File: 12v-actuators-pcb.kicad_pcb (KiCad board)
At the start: 2 copper layers, 109 x 60 mm, 105 parts, among them J1 12V_C_MOT, J10 ESC_35_2_P, J11 MOTOR_15_2, J12 ESC_35_2_S, J13 MOTOR_15_3, J14 690367280876, J2 3.5mm WR-TBL, J3 690367280676, J4 LCD_DEG, J5 CAN, J6 ESC_35_1_P, J7 LED_EN, J8 MOTOR_15_1, J9 ESC_35_1_S, Q1 G2302, Q2 G2302, Q3 G2302, Q4 G2302, Q5 G2302, Q6 SUM110P06-08L, Q7 2N7002, Q8 2N7002, U1 MCP2551-I-SN, U2 NUCLEO-F303K8, U3 WSEN-PDUS, U4 TCA9517DR, X1 ESC_Emax_Bullet_15A, X2 ESC_Emax_Bullet_15A, X3 ESC_Emax_Bullet_15A

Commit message: CDR 2025 version WIP
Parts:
- removed C15: 470pF, Capacitor_SMD:C_0603_1608Metric
- removed C3: 10uF, Capacitor_SMD:C_0805_2012Metric
- removed G*** (x5): LOGO, LOGO
- removed the J1 at (194.7, 106.4)
- removed the J4 at (154.1, 108.7)
- removed the J5 at (150.3, 103.7)
- removed REF** (x4): Mounting_Wuerth_WA-SMSI-M3_H1.5mm_9774015360, Mounting_Wuerth:Mounting_Wuerth_WA-SMSI-M3_H1.5mm_9774015360
- removed U2: NUCLEO-F303K8, ComponentsEvo:MODULE_NUCLEO-F303K8
- removed X1, X2, X3: ESC_Emax_Bullet_15A, ComponentsEvo:ESC_Emax_Bullet_15A
- added C27: 18pF, Capacitor_SMD:C_0603_1608Metric, F.Cu at (48.0, 43.6)
- added C28: 18pF, Capacitor_SMD:C_0603_1608Metric, F.Cu at (34.3, 49.6)
- added C29: 10nF, Capacitor_SMD:C_0603_1608Metric, F.Cu at (36.0, 52.9)
- added C30: 100nF, Capacitor_SMD:C_0603_1608Metric, F.Cu at (40.5, 43.6)
- added C31: 100nF, Capacitor_SMD:C_0603_1608Metric, F.Cu at (34.3, 52.9)
- added C32: 10nF, Capacitor_SMD:C_0603_1608Metric, F.Cu at (36.0, 49.6)
- added D10: ~, Diode_SMD:D_SOD-123F, F.Cu at (279.5, 126.1)
- added D11: ~, Diode_SMD:D_SOD-123F, F.Cu at (279.5, 132.9)
- added D12: ~, Diode_SMD:D_SOD-123F, F.Cu at (279.5, 96.1)
- added D13: ~, Diode_SMD:D_SOD-123F, F.Cu at (279.5, 88.4)
- added D14: ~, Diode_SMD:D_SOD-123F, F.Cu at (279.5, 80.6)
- added D15: ~, Diode_SMD:D_SOD-123F, F.Cu at (279.5, 155.9)
- added D16: ~, Diode_SMD:D_SOD-123F, F.Cu at (279.5, 148.1)
- added D17: ~, Diode_SMD:D_SOD-123F, F.Cu at (279.5, 140.1)
- added D18: ~, Diode_SMD:D_SOD-123F, F.Cu at (273.3, 50.1)
- added D9: D_Schottky, Diode_SMD:D_SOD-882, F.Cu at (214.0, 52.0)
- added J1: 690367280876, ConnectorsEvo:690367280876, F.Cu at (118.3, 68.4)
- added J1: 12V_C_MOT, ConnectorsEvo:691321100002, F.Cu at (137.0, 79.1)
- added J4: PROG, Connector_PinHeader_2.54mm:PinHeader_1x03_P2.54mm_Vertical, F.Cu at (66.8, 42.6)
- added J4: LCD_DEG, Connector_PinHeader_2.54mm:PinHeader_1x03_P2.54mm_Vertical, F.Cu at (142.0, 120.8)
- added J5: CAN, Connector_PinHeader_2.54mm:PinHeader_1x02_P2.54mm_Vertical, F.Cu at (205.0, 51.0)
- added J5: USB_B_Mini, ConnectorsEvo:USB_Mini-B_Wuerth_65100516121_Horizontal, F.Cu at (228.1, 50.5)
- added Q10: G2302, Package_TO_SOT_SMD:SOT-23, F.Cu at (276.4, 88.4)
- added Q11: G2302, Package_TO_SOT_SMD:SOT-23, F.Cu at (276.2, 80.6)
- added Q12: G2302, Package_TO_SOT_SMD:SOT-23, F.Cu at (276.3, 155.9)
- added Q13: G2302, Package_TO_SOT_SMD:SOT-23, F.Cu at (276.3, 148.1)
- added Q14: G2302, Package_TO_SOT_SMD:SOT-23, F.Cu at (276.0, 140.1)
- added Q15: G2302, Package_TO_SOT_SMD:SOT-23, F.Cu at (276.3, 96.1)
- added Q16: G2302, Package_TO_SOT_SMD:SOT-23, F.Cu at (149.0, 52.0)
- added Q17: G2302, Package_TO_SOT_SMD:SOT-23, F.Cu at (270.0, 50.1)
- added Q9: G2302, Package_TO_SOT_SMD:SOT-23, F.Cu at (276.3, 132.9)
- added R33: 10k, Resistor_SMD:R_0603_1608Metric, F.Cu at (273.5, 126.1)
- added R34: 1k, Resistor_SMD:R_0603_1608Metric, F.Cu at (271.5, 132.9)
- added R35: 10k, Resistor_SMD:R_0603_1608Metric, F.Cu at (273.3, 132.9)
- added R36: 1k, Resistor_SMD:R_0603_1608Metric, F.Cu at (271.8, 96.1)
- added R37: 1k, Resistor_SMD:R_0603_1608Metric, F.Cu at (271.8, 88.4)
- added R38: 1k, Resistor_SMD:R_0603_1608Metric, F.Cu at (271.5, 80.6)
- added R39: 1k, Resistor_SMD:R_0603_1608Metric, F.Cu at (271.8, 155.9)
- added R40: 1k, Resistor_SMD:R_0603_1608Metric, F.Cu at (271.8, 148.1)
- added R41: 1k, Resistor_SMD:R_0603_1608Metric, F.Cu at (271.3, 140.1)
- added R42: 10k, Resistor_SMD:R_0603_1608Metric, F.Cu at (273.3, 80.6)
- added R43: 10k, Resistor_SMD:R_0603_1608Metric, F.Cu at (273.5, 155.9)
- added R44: 10k, Resistor_SMD:R_0603_1608Metric, F.Cu at (273.5, 148.1)
- added R45: 10k, Resistor_SMD:R_0603_1608Metric, F.Cu at (273.0, 140.1)
- added R46: 10k, Resistor_SMD:R_0603_1608Metric, F.Cu at (273.5, 88.4)
- added R47: 10k, Resistor_SMD:R_0603_1608Metric, F.Cu at (273.5, 96.1)
- added R48: 10k, Resistor_SMD:R_0603_1608Metric, F.Cu at (152.0, 45.0)
- added R49: 0, Resistor_SMD:R_0603_1608Metric, F.Cu at (152.0, 48.0)
- added R50: 22, Resistor_SMD:R_0603_1608Metric, F.Cu at (198.0, 58.0)
- added R51: 1k, Resistor_SMD:R_0603_1608Metric, F.Cu at (265.5, 50.1)
- added R52: 10k, Resistor_SMD:R_0603_1608Metric, F.Cu at (267.3, 50.1)
- added R53: 0, Resistor_SMD:R_0402_1005Metric, F.Cu at (55.0, 50.6)
- added R54: 0, Resistor_SMD:R_0402_1005Metric, F.Cu at (41.0, 61.6)
- added R55: 0, Resistor_SMD:R_0402_1005Metric, F.Cu at (42.3, 61.6)
- added R56: 0, Resistor_SMD:R_0402_1005Metric, F.Cu at (55.0, 56.9)
- added R57: 0, Resistor_SMD:R_0402_1005Metric, F.Cu at (55.0, 58.1)
- added R58: 0, Resistor_SMD:R_0402_1005Metric, F.Cu at (48.5, 61.6)
- added R59: 0, Resistor_SMD:R_0402_1005Metric, F.Cu at (47.3, 61.6)
- added R60: 0, Resistor_SMD:R_0402_1005Metric, F.Cu at (46.0, 61.6)
- added R61: 0, Resistor_SMD:R_0402_1005Metric, F.Cu at (27.5, 49.1)
- added R62: 0, Resistor_SMD:R_0402_1005Metric, F.Cu at (43.5, 61.6)
- added R63: 0, Resistor_SMD:R_0402_1005Metric, F.Cu at (44.8, 61.6)
- added R64: 0, Resistor_SMD:R_0402_1005Metric, F.Cu at (27.5, 50.4)
- added R65: 0, Resistor_SMD:R_0402_1005Metric, F.Cu at (27.5, 51.6)
- added R66: 0, Resistor_SMD:R_0402_1005Metric, F.Cu at (27.5, 52.9)
- added R67: 0, Resistor_SMD:R_0402_1005Metric, F.Cu at (55.0, 55.6)
- added R68: 0, Resistor_SMD:R_0402_1005Metric, F.Cu at (55.0, 54.4)
- added R69: 0, Resistor_SMD:R_0402_1005Metric, F.Cu at (55.0, 53.1)
- added R70: 0, Resistor_SMD:R_0402_1005Metric, F.Cu at (55.0, 49.4)
- added R71: 0, Resistor_SMD:R_0402_1005Metric, F.Cu at (43.0, 37.1)
- added R72: 0, Resistor_SMD:R_0402_1005Metric, F.Cu at (41.8, 37.1)
- added R73: 0, Resistor_SMD:R_0402_1005Metric, F.Cu at (55.0, 51.9)
- added R74: 0, Resistor_SMD:R_0402_1005Metric, F.Cu at (27.5, 55.4)
- added R75: 0, Resistor_SMD:R_0402_1005Metric, F.Cu at (27.5, 54.1)
- added R76: 0, Resistor_SMD:R_0402_1005Metric, F.Cu at (55.0, 48.1)
- added R77: 10k, Resistor_SMD:R_0402_1005Metric, F.Cu at (233.0, 59.0)
- added R78: 0, Resistor_SMD:R_0402_1005Metric, F.Cu at (40.5, 37.1)
- added R79: 0, Resistor_SMD:R_0402_1005Metric, F.Cu at (76.4, 45.8)
- added R80: 0, Resistor_SMD:R_0402_1005Metric, F.Cu at (76.4, 47.8)
- added R81: 0, Resistor_SMD:R_0402_1005Metric, F.Cu at (76.4, 49.8)
- added SW1: 435431019840, ComponentsEvo:435431019840, F.Cu at (220.0, 46.0)
- added TP1: TestPoint_Small, TestPoint:TestPoint_Pad_D1.0mm, F.Cu at (39.5, 32.4)
- added TP10: TestPoint_Small, TestPoint:TestPoint_Pad_D1.0mm, F.Cu at (64.3, 51.6)
- added TP11: TestPoint_Small, TestPoint:TestPoint_Pad_D1.0mm, F.Cu at (48.3, 32.4)
- added TP12: TestPoint_Small, TestPoint:TestPoint_Pad_D1.0mm, F.Cu at (41.8, 68.6)
- added TP13: TestPoint_Small, TestPoint:TestPoint_Pad_D1.0mm, F.Cu at (64.3, 54.1)
- added TP14: TestPoint_Small, TestPoint:TestPoint_Pad_D1.0mm, F.Cu at (22.0, 50.6)
- added TP2: TestPoint_Small, TestPoint:TestPoint_Pad_D1.0mm, F.Cu at (41.0, 29.9)
- added TP3: TestPoint_Small, TestPoint:TestPoint_Pad_D1.0mm, F.Cu at (22.0, 47.9)
- added TP4: TestPoint_Small, TestPoint:TestPoint_Pad_D1.0mm, F.Cu at (22.0, 53.4)
- added TP5: TestPoint_Small, TestPoint:TestPoint_Pad_D1.0mm, F.Cu at (41.8, 66.4)
- added TP6: TestPoint_Small, TestPoint:TestPoint_Pad_D1.0mm, F.Cu at (38.8, 68.6)
- added TP7: TestPoint_Small, TestPoint:TestPoint_Pad_D1.0mm, F.Cu at (44.8, 68.6)
- added TP8: TestPoint_Small, TestPoint:TestPoint_Pad_D1.0mm, F.Cu at (45.3, 32.4)
- added TP9: TestPoint_Small, TestPoint:TestPoint_Pad_D1.0mm, F.Cu at (42.5, 32.4)
- added U5: STM32G474CEUx, Package_DFN_QFN:QFN-48-1EP_7x7mm_P0.5mm_EP5.6x5.6mm, F.Cu at (43.8, 52.4)
- added U6: TPS82130, Goldorak:MicroSiP, F.Cu at (56.8, 119.9)
- added U7: AMS1117-3.3, Package_TO_SOT_SMD:SOT-89-3, F.Cu at (209.0, 62.0)
- added Y1: 16 MHz, Crystal:Crystal_SMD_5032-4Pin_5.0x3.2mm, F.Cu at (44.3, 43.6)
- C12: value 470pF -> 10uF
- C14, C4: value 100nF -> 10uF
- C7: value 470pF -> 430pF
- C9: value 100nF -> 22uF
- D1: value ~ -> D_Schottky; footprint Diode_SMD:D_SOD-123F -> Diode_SMD:D_SOD-882
- J10: value ESC_35_2_P -> ESC_35_1_P
- J11: value MOTOR_15_2 -> 690367280876; footprint Connector_PinHeader_2.54mm:PinHeader_1x03_P2.54mm_Vertical -> ConnectorsEvo:690367280876
- J13: value MOTOR_15_3 -> STLINK; footprint Connector_PinHeader_2.54mm:PinHeader_1x03_P2.54mm_Vertical -> ConnectorsEvo:SAMTEC_FTSH-107-01-L-DV-K
- J7: value LED_EN -> RGBA_LEDs; footprint Connector_PinHeader_2.54mm:PinHeader_1x02_P2.54mm_Vertical -> Connector_PinHeader_2.54mm:PinHeader_1x03_P2.54mm_Vertical
- J8: value MOTOR_15_1 -> CAN
- R12: value 22 -> 1k
- R3: value 22 -> 100k
- R4: value 1k -> 523k
- R5: value 10k -> 100k
- R7: value 22 -> 10k
- moved D2 147.8 mm to (279.5, 111.6), turned to 90 degrees
- moved D3 147.2 mm to (279.5, 119.1), turned to -90 degrees
- moved Q2 145.9 mm to (276.3, 111.6), turned to 0 degrees
- moved Q3 143.9 mm to (276.3, 119.1), turned to 0 degrees
- moved R9 142.0 mm to (273.5, 111.6)
- moved R8 141.7 mm to (271.8, 111.6)
- moved R13 139.8 mm to (273.5, 119.1)
- moved R11 139.6 mm to (271.8, 119.1), turned to 90 degrees
- moved D4 137.0 mm to (278.8, 70.6), turned to 90 degrees
- moved C23 136.0 mm to (231.0, 40.0), turned to 0 degrees
- moved D5 135.8 mm to (279.5, 104.1), turned to 90 degrees
- moved Q4 134.6 mm to (275.5, 70.6), turned to 0 degrees
- moved Q5 132.0 mm to (276.3, 104.1), turned to 0 degrees
- moved R15 131.7 mm to (272.8, 70.6)
- moved R14 131.4 mm to (271.0, 70.6)
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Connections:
- net /A_PRES renamed /Capteurs/A_PRES
- C1 pad 2: +5V -> +5VL
- C12 pad 1: Net-(X2-S) -> +5VL
- C14 pad 1: GNDPWR -> +3.3V
- C14 pad 2: /PWR_12V -> GND
- C20 pad 1: +5V -> +5VL
- C24 pad 1: +5V -> +5VL
- C4 pad 1: GNDPWR -> /VBATT_12V
- C4 pad 2: /PWR_12V -> GND
- C7 pad 1: Net-(X1-S) -> Net-(U6-SS/TR)
- C7 pad 2: GND -> GNDPWR
- C9 pad 1: GNDPWR -> +5VP
- C9 pad 2: /PWR_12V -> GNDPWR
- D1 pad 1: /PWR_12V -> +5VL
- D1 pad 2: Net-(D1-A) -> /5V_CAN
- J11 pad 1: Net-(J11-Pin_1) -> /PWR_12V
- J11 pad 2: Net-(J11-Pin_2) -> /Actionneurs/12V_EV8
- J11 pad 3: Net-(J11-Pin_3) -> /PWR_12V
- J13 pad 1: Net-(J13-Pin_1) -> unconnected-(J13-Pin_1-Pad1)
- J13 pad 2: Net-(J13-Pin_2) -> unconnected-(J13-Pin_2-Pad2)
- J13 pad 3: Net-(J13-Pin_3) -> +3.3V
- J14 pad 7: /PWR_12V -> /VBATT_12V
- J6 pad 2: GNDPWR -> Net-(J6-Pin_2)
- J7 pad 1: Net-(D1-A) -> +5VP
- J7 pad 2: /PWR_12V -> /DATA_LED
- J8 pad 1: Net-(J8-Pin_1) -> /CAN+
- J8 pad 2: Net-(J8-Pin_2) -> /CAN-
- J8 pad 3: Net-(J8-Pin_3) -> /5V_CAN
- Q1 pad 3: Net-(D1-A) -> /Actionneurs/12V_EV4
- R12 pad 1: /DS_M3 -> Net-(Q1-G)
- R12 pad 2: Net-(X3-S) -> /EV_4
- R25 pad 1: +5V -> +5VL
- R26 pad 1: +5V -> +5VL
- R3 pad 1: /DS_M1 -> +5VP
- R3 pad 2: Net-(X1-S) -> Net-(U6-PG)
- R4 pad 1: Net-(Q1-G) -> Net-(U6-FB)
- R4 pad 2: /LED_EN -> +5VP
- R5 pad 1: Net-(Q1-G) -> GNDPWR
- R5 pad 2: GNDPWR -> Net-(U6-FB)
- R7 pad 1: /DS_M2 -> GNDPWR
- R7 pad 2: Net-(X2-S) -> +5VL
- U1 pad 1: /CAN_TD -> /CAN_TX
- U1 pad 3: +5V -> +5VL
- U1 pad 4: /CAN_RD -> /CAN_RX
- U3 pad 5: +5V -> +5VL
- U4 pad 8: +5V -> +5VL
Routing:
- net GND: track 334.5 -> 0.00 mm, vias 69 -> 0
- net +5V: track 149.1 -> 0.00 mm, vias 6 -> 0
- net /PWR_12V: track 121.8 -> 0.00 mm, vias 7 -> 0
- net /VBATT_12V: track 116.2 -> 0.00 mm, vias 3 -> 0
- net +3.3V: track 111.6 -> 0.00 mm, vias 3 -> 0
- net /EV_P: track 87.7 -> 0.00 mm
- net /DS_COMP: track 77.7 -> 0.00 mm, vias 3 -> 0
- net GNDPWR: track 72.0 -> 0.00 mm, vias 13 -> 0
- net /DS_M1: track 64.2 -> 0.00 mm, vias 2 -> 0
- net /EV_3: track 62.1 -> 0.00 mm
- net /CAN_TD: track 57.1 -> 0.00 mm, vias 1 -> 0
- net /SDA: track 57.0 -> 0.00 mm
- net /EV_2: track 56.6 -> 0.00 mm
- net Net-(X1-S): track 55.3 -> 0.00 mm, vias 1 -> 0
- net /EV_1: track 49.9 -> 0.00 mm
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- removed copper zone on F.Cu, net /PWR_12V
- removed copper zone on F.Cu, net /VBATT_12V
- removed copper zone on B.Cu, net GND
- removed copper zone on F.Cu, net GND
- removed copper zone on B.Cu, net GNDPWR
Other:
- board size 109 x 60 mm -> 100 x 60 mm
- board text removed: "+"
- board text removed: "-"
- board text removed: "12V BATT"
- board text removed: "24V"
- board text removed: "5V"
- board text removed: "AU Switched 12V"
- board text removed: "BATT"
- board text removed: "BRUSHLESS MOTOR OUTPUT"
- board text removed: "CANH"
- board text removed: "CANL"
- board text removed: "COMP"
- board text removed: "Carte pneumatique / Actionneurs 12V"
- board text removed: "Carte pneumatique Actionneurs 12V"
- board text removed: "DROITE"
- board text removed: "Design: Raphaël Casimir Review: Audran Caron Thanks: kmikaz"
- board text removed: "EN"
- board text removed: "ESC"
- board text removed: "EV1"
- board text removed: "EV2"
- board text removed: "EV3"
- board text removed: "G"
- board text removed: "GAUCHE"
- board text removed: "GND"
- board text removed: "G_L"
- board text removed: "G_P"
- board text removed: "H-BRG"
- board text removed: "IN"
- board text removed: "LED"
- board text removed: "MILIEU"
- board text removed: "OUT"
- board text removed: "PRG"
- board text removed: "S"
- board text removed: "TURB"
- board text removed: "VCC"
- board text removed: "X 5 AU G X X"
- board text removed: "clavier"

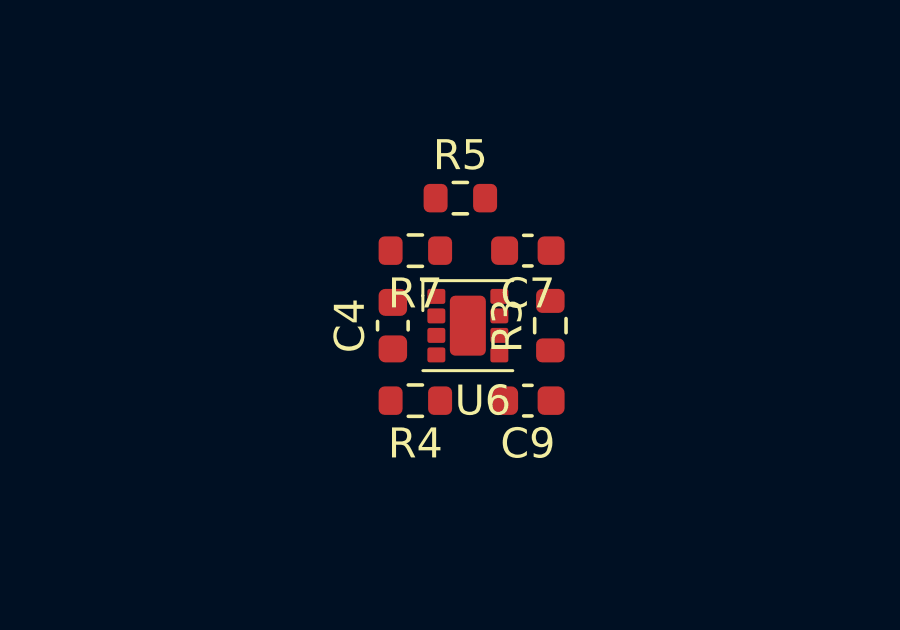
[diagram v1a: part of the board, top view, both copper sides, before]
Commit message: split des cartes
Todo: sync routage et ajout trou de fixation
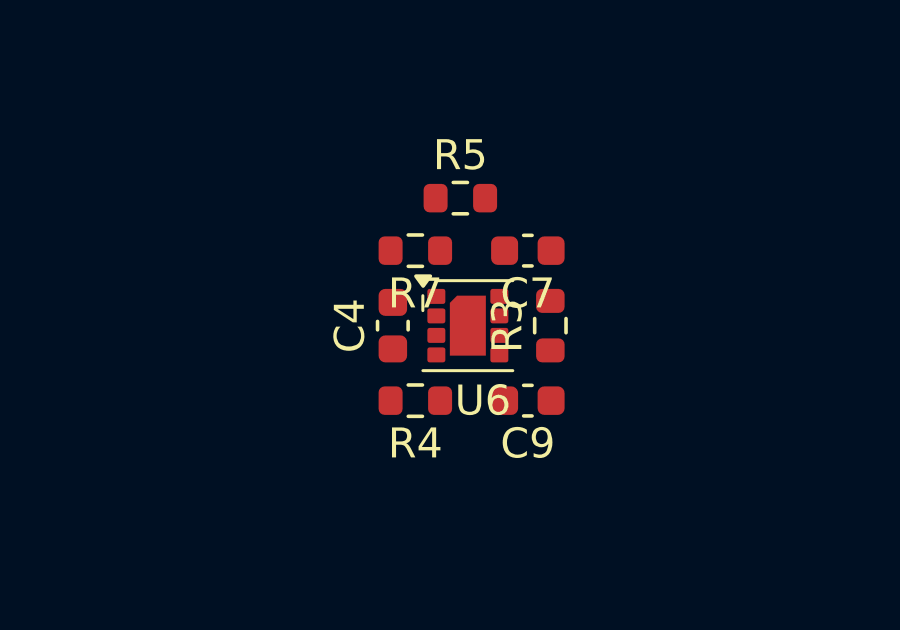
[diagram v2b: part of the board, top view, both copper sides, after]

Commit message: ajout d'une lib projet et synchro PCB
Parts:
- removed C31: 100nF, Capacitor_SMD:C_0603_1608Metric
- removed C32: 10nF, Capacitor_SMD:C_0603_1608Metric
- removed D11: ~, Diode_SMD:D_SOD-123F
- removed the J1 at (118.3, 68.4)
- removed the J4 at (66.8, 42.6)
- removed the J5 at (205.0, 51.0)
- removed Q9: G2302, Package_TO_SOT_SMD:SOT-23
- removed R34: 1k, Resistor_SMD:R_0603_1608Metric
- removed R35: 10k, Resistor_SMD:R_0603_1608Metric
- removed TP10, TP11, TP12, TP13, TP14, TP9: TestPoint_Small, TestPoint:TestPoint_Pad_D1.0mm
- removed U7: AMS1117-3.3, Package_TO_SOT_SMD:SOT-89-3
- added C15: 18pF, Capacitor_SMD:C_0603_1608Metric, F.Cu at (69.1, 157.0)
- added C3: 100nF, Capacitor_SMD:C_0603_1608Metric, F.Cu at (69.1, 154.5)
- added D19: ~, Diode_SMD:D_SOD-123F, F.Cu at (53.6, 172.9)
- added J15: BOOT0, Connector_PinHeader_2.54mm:PinHeader_1x02_P2.54mm_Vertical, F.Cu at (73.4, 155.6)
- added J16: 690367280876, ConnectorsEvo:690367280876, F.Cu at (39.4, 179.2)
- added J17: 690367280876, ConnectorsEvo:690367280676, F.Cu at (56.5, 157.7)
- added J18: 690367280876, ConnectorsEvo:690367280676, F.Cu at (56.5, 166.7)
- added J19: Alim EV, Connector_PinSocket_2.54mm:PinSocket_1x02_P2.54mm_Vertical, F.Cu at (34.8, 155.6)
- added J20: Alim EV, Connector_PinSocket_2.54mm:PinSocket_1x02_P2.54mm_Vertical, F.Cu at (39.4, 155.6)
- added J21: Alim EV, Connector_PinSocket_2.54mm:PinSocket_1x02_P2.54mm_Vertical, F.Cu at (44.0, 155.6)
- added J22: Alim EV, Connector_PinSocket_2.54mm:PinSocket_1x02_P2.54mm_Vertical, F.Cu at (48.5, 155.6)
- added J23: Alim EV, Connector_PinSocket_2.54mm:PinSocket_1x02_P2.54mm_Vertical, F.Cu at (34.8, 162.7)
- added J24: Alim EV, Connector_PinSocket_2.54mm:PinSocket_1x02_P2.54mm_Vertical, F.Cu at (39.4, 162.7)
- added J25: Alim EV, Connector_PinSocket_2.54mm:PinSocket_1x02_P2.54mm_Vertical, F.Cu at (44.0, 162.7)
- added J26: Alim EV, Connector_PinSocket_2.54mm:PinSocket_1x02_P2.54mm_Vertical, F.Cu at (48.5, 162.7)
- added J27: Alim EV, Connector_PinSocket_2.54mm:PinSocket_1x02_P2.54mm_Vertical, F.Cu at (34.8, 169.8)
- added J28: Alim EV, Connector_PinSocket_2.54mm:PinSocket_1x02_P2.54mm_Vertical, F.Cu at (39.4, 169.8)
- added J29: Alim EV, Connector_PinSocket_2.54mm:PinSocket_1x02_P2.54mm_Vertical, F.Cu at (44.0, 169.8)
- added J30: Alim EV, Connector_PinSocket_2.54mm:PinSocket_1x02_P2.54mm_Vertical, F.Cu at (48.5, 169.8)
- added Q18: G2302, Package_TO_SOT_SMD:SOT-23, F.Cu at (57.3, 177.0)
- added R82: 10k, Resistor_SMD:R_0603_1608Metric, F.Cu at (69.1, 159.5)
- added R83: 0, Resistor_SMD:R_0402_1005Metric, F.Cu at (65.6, 154.2)
- added R84: 0, Resistor_SMD:R_0402_1005Metric, F.Cu at (65.6, 156.2)
- added R85: 0, Resistor_SMD:R_0402_1005Metric, F.Cu at (65.6, 158.2)
- added R86: 0, Resistor_SMD:R_0402_1005Metric, F.Cu at (65.6, 160.2)
- added R87: 1k, Resistor_SMD:R_0603_1608Metric, F.Cu at (52.8, 175.8)
- added R88: 10k, Resistor_SMD:R_0603_1608Metric, F.Cu at (52.8, 178.3)
- added U2: TCA9517DR, Package_SO:SOIC-8_3.9x4.9mm_P1.27mm, F.Cu at (71.3, 164.1)
- C12: value 10uF -> 100nF
- C14: value 10uF -> 18pF
- C20: value 220nF -> 10nF
- C21: value 15nF -> 100nF
- C24: value 100nF -> 220nF
- C25: value 100nF -> 10nF
- C26: value 1uF -> 15nF; footprint Capacitor_SMD:C_0805_2012Metric -> Capacitor_SMD:C_0603_1608Metric
- C27: value 18pF -> 100nF
- C28: value 18pF -> 1uF; footprint Capacitor_SMD:C_0603_1608Metric -> Capacitor_SMD:C_0805_2012Metric
- C29: value 10nF -> 10uF
- C30: value 100nF -> 10uF
- J1: value 12V_C_MOT -> 690367280876; footprint ConnectorsEvo:691321100002 -> ConnectorsEvo:690367280676
- J11: footprint ConnectorsEvo:690367280876 -> ConnectorsEvo:690367280676
- J13: value STLINK -> Alim Pompe; footprint ConnectorsEvo:SAMTEC_FTSH-107-01-L-DV-K -> Connector_PinHeader_2.54mm:PinHeader_1x02_P2.54mm_Vertical
- J4: value LCD_DEG -> STLINK; footprint Connector_PinHeader_2.54mm:PinHeader_1x03_P2.54mm_Vertical -> ConnectorsEvo:SAMTEC_FTSH-107-01-L-DV-K
- J8: footprint Connector_PinHeader_2.54mm:PinHeader_1x03_P2.54mm_Vertical -> Connector_PinHeader_2.54mm:PinHeader_1x04_P2.54mm_Vertical
- R27: value 22 -> 10k
- R29: value 10k -> 0; footprint Resistor_SMD:R_0603_1608Metric -> Resistor_SMD:R_0402_1005Metric
- R3: value 100k -> 10k
- R30, R31: value 100k -> 0; footprint Resistor_SMD:R_0603_1608Metric -> Resistor_SMD:R_0402_1005Metric
- R32: value 22 -> 0; footprint Resistor_SMD:R_0603_1608Metric -> Resistor_SMD:R_0402_1005Metric
- R4: value 523k -> 100k
- R5: value 100k -> 523k
- R64, R80: value 0 -> 22; footprint Resistor_SMD:R_0402_1005Metric -> Resistor_SMD:R_0603_1608Metric
- R7: value 10k -> 100k
- R77: value 10k -> 0
- R78, R79: value 0 -> 100k; footprint Resistor_SMD:R_0402_1005Metric -> Resistor_SMD:R_0603_1608Metric
- R81: value 0 -> 10k
- U4: value TCA9517DR -> STM32G474CEUx; footprint Package_SO:SOIC-8_3.9x4.9mm_P1.27mm -> Package_DFN_QFN:QFN-48-1EP_7x7mm_P0.5mm_EP5.6x5.6mm
- U5: value STM32G474CEUx -> AMS1117-3.3; footprint Package_DFN_QFN:QFN-48-1EP_7x7mm_P0.5mm_EP5.6x5.6mm -> Package_TO_SOT_SMD:SOT-89-3
- U6: footprint Goldorak:MicroSiP -> 12V-actuators_pcb:MicroSiP
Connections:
- net /Arrêt d'urgence/SW_AU/2 renamed /Alim et Arrêt d'urgence/SW_AU/2
- C14 pad 1: +3.3V -> GND
- C14 pad 2: GND -> Net-(U4-PF0)
- C20 pad 1: +5VL -> +3.3V
- C21 pad 1: Net-(U3-VOUT) -> +3.3V
- C22 pad 1: /Capteurs/A_PRES -> Net-(U3-VOUT)
- C25 pad 1: GND -> +3.3V
- C25 pad 2: Net-(C25-Pad2) -> GND
- C26 pad 1: GND -> /MCU et capteurs/A_PRES
- C26 pad 2: /A_TEMP -> GND
- C27 pad 2: Net-(U5-PF0) -> Net-(C27-Pad2)
- C28 pad 2: Net-(U5-PF1) -> /MCU et capteurs/A_TEMP
- C29 pad 1: +3.3V -> +5VL
- C4 pad 2: GND -> GNDPWR
- D1 pad 2: /5V_CAN -> /5L
- J11 pad 2: /Actionneurs/12V_EV8 -> GNDPWR
- J11 pad 3: /PWR_12V -> /EV_9
- J11 pad 4: /Actionneurs/12V_EV9 -> /EV_10
- J11 pad 5: /PWR_12V -> /EV_11
- J11 pad 6: /Actionneurs/12V_EV10 -> unconnected-(J11-Pad6)
- J13 pad 1: unconnected-(J13-Pin_1-Pad1) -> /PWR_12V
- J13 pad 2: unconnected-(J13-Pin_2-Pad2) -> /Actionneurs/12V_VAC
- J14 pad 2: /Actionneurs/12V_EV1 -> GNDPWR
- J14 pad 3: /PWR_12V -> /VBATT_12V
- J14 pad 4: /Actionneurs/12V_EV2 -> /EV_P
- J14 pad 5: /PWR_12V -> /EV_1
- J14 pad 6: /Actionneurs/12V_EV3 -> /EV_2
- J14 pad 7: /VBATT_12V -> /EV_3
- J14 pad 8: /Actionneurs/12V_EVP -> /EV_4
- J3 pad 3: +5V -> /5L
- J4 pad 1: /SW_AU -> unconnected-(J4-Pin_1-Pad1)
- J4 pad 2: GNDPWR -> unconnected-(J4-Pin_2-Pad2)
- J4 pad 3: /LCD_EN -> +3.3V
- J8 pad 1: /CAN+ -> /5L
- J8 pad 2: /CAN- -> GND
- J8 pad 3: /5V_CAN -> /CANH
- R1 pad 1: /CAN+ -> /CANH
- R2 pad 2: /CAN- -> /CANL
- R25 pad 1: +5VL -> +3.3V
- R25 pad 2: /Capteurs/SDA_5 -> /MCU et capteurs/SCL
- R26 pad 1: +5VL -> +3.3V
- R26 pad 2: /Capteurs/SCL_5 -> /MCU et capteurs/SDA
- R27 pad 1: Net-(U3-VOUT) -> +5VL
- R27 pad 2: /Capteurs/A_PRES -> /MCU et capteurs/SDA_5
- R28 pad 1: +3.3V -> +5VL
- R28 pad 2: /SCL -> /MCU et capteurs/SCL_5
- R29 pad 1: +3.3V -> /EV_4
- R29 pad 2: /SDA -> Net-(U4-PC15)
- R3 pad 1: +5VP -> GNDPWR
- R3 pad 2: Net-(U6-PG) -> +5VL
- R30 pad 1: +3.3V -> /EV_1
- R30 pad 2: Net-(C25-Pad2) -> Net-(U4-PB0)
- R31 pad 1: +3.3V -> /EV_2
- R31 pad 2: Net-(C25-Pad2) -> Net-(U4-PB1)
- R32 pad 1: Net-(C25-Pad2) -> /EV_3
- R32 pad 2: /A_TEMP -> Net-(U4-PB2)
- R4 pad 1: Net-(U6-FB) -> +5VP
- R4 pad 2: +5VP -> Net-(U6-PG)
- R5 pad 1: GNDPWR -> Net-(U6-FB)
- R5 pad 2: Net-(U6-FB) -> +5VP
- R53 pad 1: /SDA -> /MCU et capteurs/SWO
- R53 pad 2: Net-(U5-PB7) -> Net-(U4-PB3)
- R54 pad 1: /CAN_RX -> /EV_5
- R54 pad 2: Net-(U5-PB12) -> Net-(U4-PB4)
- R55 pad 1: /CAN_TX -> /EV_6
- R55 pad 2: Net-(U5-PB13) -> Net-(U4-PB5)
- R56 pad 1: Net-(U5-PA15) -> /EV_7
- R56 pad 2: /SCL -> Net-(U4-PB6)
- R57 pad 1: Net-(U5-PA14) -> /MCU et capteurs/SDA
- R57 pad 2: /MCU/SWTCK -> Net-(U4-PB7)
- R58 pad 1: Net-(U5-PA13) -> /MCU et capteurs/BOOT0
- R58 pad 2: /MCU/SWDIO -> Net-(U4-PB8)
- R59 pad 1: Net-(U5-PA12) -> /EV_8
- R59 pad 2: /USB_DP -> Net-(U4-PB9)
- R60 pad 1: Net-(U5-PA11) -> /EV_9
- R60 pad 2: /USB_DN -> Net-(U4-PB10)
- R61 pad 1: Net-(U5-PA5) -> /EV_10
- R61 pad 2: /DATA_LED -> Net-(U4-PB11)
- R62 pad 1: Net-(U5-PA8) -> /CAN_RX
- R62 pad 2: /DS_TURB -> Net-(U4-PB12)
- R63 pad 1: Net-(U5-PA9) -> /CAN_TX
- R63 pad 2: /DS_COMP -> Net-(U4-PB13)
- R64 pad 1: /EV_1 -> Net-(U3-VOUT)
- R64 pad 2: Net-(U5-PB0) -> /MCU et capteurs/A_PRES
- R65 pad 1: /EV_2 -> Net-(U4-PA0)
- R65 pad 2: Net-(U5-PB1) -> /MCU et capteurs/A_TEMP
- R66 pad 1: /EV_3 -> Net-(U4-PA1)
- R66 pad 2: Net-(U5-PB2) -> /MCU et capteurs/A_PRES
- R67 pad 1: /MCU/SWO -> Net-(U4-PA2)
- R67 pad 2: Net-(U5-PB3) -> /MCU et capteurs/VCP_TX
- R68 pad 1: /EV_5 -> Net-(U4-PA3)
- R68 pad 2: Net-(U5-PB4) -> /MCU et capteurs/VCP_RX
- R69 pad 1: /EV_6 -> Net-(U4-PA4)
- R69 pad 2: Net-(U5-PB5) -> /EV_11
- R7 pad 2: +5VL -> Net-(U6-FB)
- R70 pad 1: /MCU/BOOT0 -> Net-(U4-PA5)
- R70 pad 2: Net-(U5-PB8) -> /DATA_LED
- R71 pad 1: Net-(U5-PA0) -> Net-(U4-PA9)
- R71 pad 2: /VAC -> /DS_COMP
- R72 pad 1: Net-(U5-PA1) -> Net-(U4-PA10)
- R72 pad 2: /EV_P -> /AU_STATUS
- R73 pad 1: /EV_7 -> Net-(U4-PA11)
- R73 pad 2: Net-(U5-PB6) -> /USB_DN
- R74 pad 1: /EV_10 -> Net-(U4-PA12)
- R74 pad 2: Net-(U5-PB11) -> /USB_DP
- R75 pad 1: /EV_9 -> Net-(U4-PA13)
- R75 pad 2: Net-(U5-PB10) -> /MCU et capteurs/SWDIO
- R76 pad 1: /EV_8 -> Net-(U4-PA14)
- R76 pad 2: Net-(U5-PB9) -> /MCU et capteurs/SWTCK
- R77 pad 1: /MCU/NRST -> Net-(U4-PA15)
- R77 pad 2: +3.3V -> /MCU et capteurs/SCL
- R78 pad 1: Net-(U5-PA2) -> +3.3V
- R78 pad 2: /MCU/VCP_TX -> Net-(C27-Pad2)
- R79 pad 1: /EV_4 -> +3.3V
- R79 pad 2: Net-(U5-PC15) -> Net-(C27-Pad2)
- R80 pad 1: Net-(U5-PA4) -> Net-(C27-Pad2)
- R80 pad 2: /EV_11 -> /MCU et capteurs/A_TEMP
- R81 pad 1: Net-(U5-PA3) -> /MCU et capteurs/NRST
- R81 pad 2: /MCU/VCP_RX -> +3.3V
- SW1 pad 1: /MCU/NRST -> /MCU et capteurs/NRST
- SW1 pad 4: /MCU/NRST -> /MCU et capteurs/NRST
- TH1 pad 1: Net-(C25-Pad2) -> Net-(C27-Pad2)
- TP1 pad 1: Net-(U5-PA4) -> Net-(U4-PC4)
- TP2 pad 1: Net-(U5-PA3) -> Net-(U4-PC6)
- TP3 pad 1: Net-(U5-PA6) -> Net-(U4-PC10)
- TP4 pad 1: Net-(U5-PA7) -> Net-(U4-PC11)
- TP5 pad 1: Net-(U5-PB15) -> Net-(U4-PC13)
- TP6 pad 1: Net-(U5-PB14) -> Net-(U4-PC14)
- TP7 pad 1: Net-(U5-PA10) -> Net-(U4-PB14)
- TP8 pad 1: Net-(U5-PC14) -> Net-(U4-PB15)
- U1 pad 6: /CAN- -> /CANL
- U1 pad 7: /CAN+ -> /CANH
- U3 pad 1: /Capteurs/SCL_5 -> /MCU et capteurs/SCL_5
- U3 pad 2: /Capteurs/SDA_5 -> /MCU et capteurs/SDA_5
- U4 pad 1: +3.3V -> unconnected-(U4-VBAT-Pad1)
- U4 pad 2: /SCL -> Net-(U4-PC13)
- U4 pad 3: /SDA -> Net-(U4-PC14)
- U4 pad 4: GND -> Net-(U4-PC15)
- U4 pad 5: +5V -> Net-(U4-PF0)
- U4 pad 6: /Capteurs/SDA_5 -> Net-(U4-PF1)
- U4 pad 7: /Capteurs/SCL_5 -> /MCU et capteurs/NRST
- U4 pad 8: +5VL -> Net-(U4-PA0)
- U5 pad 1: unconnected-(U5-VBAT-Pad1) -> GND
- U5 pad 2: Net-(U5-PC13) -> +3.3V
- U5 pad 3: Net-(U5-PC14) -> +5VL
- Y1 pad 1: Net-(U5-PF0) -> Net-(U4-PF0)
- Y1 pad 3: Net-(U5-PF1) -> Net-(U4-PF1)

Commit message: optimisation empreinte passif (TODO fp diode), TODO ajouter LED temoin diverse, groupement sur PCB des nouveaux composant
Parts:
- added R34: 10k, Resistor_SMD:R_0603_1608Metric, F.Cu at (51.3, 118.1)
- added R35: 0, Resistor_SMD:R_0402_1005Metric, F.Cu at (55.0, 61.1)
- added R89: 0, NetTie:NetTie-2_SMD_Pad0.5mm, F.Cu at (159.8, 147.9)
- R19: footprint Resistor_SMD:R_0603_1608Metric -> Resistor_SMD:R_0402_1005Metric
- R24: footprint Capacitor_SMD:C_0603_1608Metric -> NetTie:NetTie-2_SMD_Pad0.5mm
- R49: footprint Resistor_SMD:R_0603_1608Metric -> Jumper:SolderJumper-2_P1.3mm_Open_RoundedPad1.0x1.5mm
- moved J28 346.4 mm to (352.3, 21.2), turned to 90 degrees
- moved J29 344.3 mm to (352.3, 16.6), turned to 90 degrees
- moved J30 342.3 mm to (352.3, 12.0), turned to 90 degrees
- moved J27 336.6 mm to (353.1, 60.5), turned to -90 degrees
- moved J24 332.5 mm to (353.5, 53.9), turned to -90 degrees
- moved J19 323.9 mm to (353.8, 99.6), turned to -90 degrees
- moved J25 322.8 mm to (354.8, 75.6), turned to -90 degrees
- moved J23 322.6 mm to (353.8, 115.1), turned to -90 degrees
- moved J26 319.6 mm to (353.8, 68.1), turned to -90 degrees
- moved J20 317.3 mm to (353.0, 107.6), turned to -90 degrees
- moved D19 315.0 mm to (345.3, 53.9), turned to 90 degrees
- moved R87 311.3 mm to (339.3, 53.9), turned to -90 degrees
- moved J21 310.8 mm to (353.5, 128.4), turned to -90 degrees
- moved R88 310.7 mm to (337.5, 53.9), turned to -90 degrees
- moved Q18 310.0 mm to (341.8, 53.9)
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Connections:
- J14 pad 3: /VBATT_12V -> /EV_1
- J14 pad 4: /EV_P -> /EV_2
- J14 pad 5: /EV_1 -> /EV_3
- J14 pad 6: /EV_2 -> /EV_4
- J14 pad 7: /EV_3 -> /VBATT_12V
- J14 pad 8: /EV_4 -> /EV_P
- J16 pad 3: /VBATT_12V -> /EV_1
- J16 pad 4: /EV_P -> /EV_2
- J16 pad 5: /EV_1 -> /EV_3
- J16 pad 6: /EV_2 -> /EV_4
- J16 pad 7: /EV_3 -> /VBATT_12V
- J16 pad 8: /EV_4 -> /EV_P
- R24 pad 1: GND -> GNDPWR
- R24 pad 2: GNDPWR -> GND
- R3 pad 2: +5VL -> /LED_EN
- R49 pad 1: GNDPWR -> Net-(J6-Pin_2)
- R49 pad 2: Net-(J6-Pin_2) -> GNDPWR
- U6 pad 1: +5VL -> /LED_EN

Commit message: placement en cours, remplacement diode schotcky, customisation empreinte capteur pression, suppression R pour les signaux figé du uC (SW, BOOT, etc). TODO avancer placement, ajouter LED
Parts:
- removed R53, R58, R75, R76: 0, Resistor_SMD:R_0402_1005Metric
- removed TP8: TestPoint_Small, TestPoint:TestPoint_Pad_D1.0mm
- added H1: MountingHole_Pad, MountingHole:MountingHole_3.2mm_M3_Pad, F.Cu at (229.3, 93.1)
- added H10: MountingHole_Pad, MountingHole:MountingHole_3.2mm_M3_Pad, F.Cu at (-95.7, 48.8)
- added H2: MountingHole_Pad, MountingHole:MountingHole_3.2mm_M3_Pad, F.Cu at (229.3, 51.1)
- added H3: MountingHole_Pad, MountingHole:MountingHole_3.2mm_M3_Pad, F.Cu at (167.3, 51.1)
- added H4: MountingHole_Pad, MountingHole:MountingHole_3.2mm_M3_Pad, F.Cu at (167.3, 93.1)
- added H5: MountingHole_Pad, MountingHole:MountingHole_3.2mm_M3_Pad, F.Cu at (-91.5, 131.9)
- added H6: MountingHole_Pad, MountingHole:MountingHole_3.2mm_M3_Pad, F.Cu at (-91.5, 139.8)
- added H7: MountingHole_Pad, MountingHole:MountingHole_3.2mm_M3_Pad, F.Cu at (-90.7, 86.1)
- added H8: MountingHole_Pad, MountingHole:MountingHole_3.2mm_M3_Pad, F.Cu at (-90.7, 94.1)
- added H9: MountingHole_Pad, MountingHole:MountingHole_3.2mm_M3_Pad, F.Cu at (-95.7, 40.9)
- D1, D9: value D_Schottky -> 1N5819WS; footprint Diode_SMD:D_SOD-882 -> Diode_SMD:D_SOD-323_HandSoldering
- D7: footprint Diode_SMD:D_SOD-323 -> Diode_SMD:D_SOD-323_HandSoldering
- moved D10 459.2 mm to (-113.5, 147.6)
- moved D12 459.2 mm to (-113.0, 101.8)
- moved D13 459.2 mm to (-113.0, 94.1)
- moved D14 459.2 mm to (-113.0, 86.3)
- moved D15 459.2 mm to (-113.2, 50.8)
- moved D16 459.2 mm to (-113.2, 43.1)
- moved D17 459.2 mm to (-113.2, 35.1)
- moved D19 459.2 mm to (-113.2, 79.8)
- moved D2 459.2 mm to (-113.5, 133.1)
- moved D3 459.2 mm to (-113.5, 140.6)
- moved D4 459.2 mm to (-114.5, 154.8)
- moved D5 459.2 mm to (-113.5, 125.6)
- moved J16 459.2 mm to (-131.7, 140.6)
- moved J17 459.2 mm to (-130.0, 94.3)
- moved J18 459.2 mm to (-131.7, 43.1)
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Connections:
- U4 pad 36: Net-(U4-PA13) -> /MCU et capteurs/SWDIO
- U4 pad 37: Net-(U4-PA14) -> /MCU et capteurs/SWTCK
- U4 pad 41: Net-(U4-PB3) -> /MCU et capteurs/SWO
- U4 pad 46: Net-(U4-PB8) -> /MCU et capteurs/BOOT0
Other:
- board size 100 x 60 mm -> 70 x 50 mm

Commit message: placement composant (carte distributeur)
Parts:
- J19, J20, J21, J22, J23, J24, J25, J26, J27, J28, J29, J30: footprint Connector_PinSocket_2.54mm:PinSocket_1x02_P2.54mm_Vertical -> 12V-actuators_pcb:PinSocket_1x02_P2.54mm_Vertical_widePad
- U4: footprint Package_DFN_QFN:QFN-48-1EP_7x7mm_P0.5mm_EP5.6x5.6mm -> 12V-actuators_pcb:QFN-48-1EP_7x7mm_P0.5mm_EP5.5x5.5mm
- moved J16 145.9 mm to (-6.05, 66.5)
- moved J17 136.5 mm to (-6.00, 151.5)
- moved R16 133.7 mm to (-8.00, 54.5), turned to 0 degrees
- moved R37 129.8 mm to (-8.00, 158.5), turned to 0 degrees
- moved D5 129.6 mm to (-3.55, 57.0), turned to -90 degrees
- moved Q5 129.3 mm to (-7.05, 57.0)
- moved J18 129.3 mm to (-6.00, 13.0)
- moved R36 129.2 mm to (-8.00, 165.0), turned to 0 degrees
- moved R17 129.1 mm to (-10.1, 57.0), turned to -90 degrees
- moved R11 128.4 mm to (-8.00, 80.0), turned to 0 degrees
- moved R12 128.4 mm to (-8.00, 87.0), turned to 0 degrees
- moved D13 128.3 mm to (-3.50, 161.0), turned to -90 degrees
- moved Q10 128.0 mm to (-7.00, 161.0)
- moved R46 127.9 mm to (-10.0, 161.0)
- moved R14 127.8 mm to (-8.00, 97.5), turned to 0 degrees
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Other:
- board size 70 x 50 mm -> 245.9 x 197.5 mm
